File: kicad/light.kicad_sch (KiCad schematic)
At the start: 152 parts, among them J2 USB_C_Receptacle_USB2.0_16P, J3 Barrell Jack, J4 02x04, J5 SM03B-SRSS-TB, J6 SM03B-SRSS-TB, J9 Conn_01x09_MountingPin, Q1 IRLML6344, Q2 IRLML6344, Q3 IRLML6344, SW1 Boot, SW3 On/Off, SW4 Mode, U1 RP2350A-QFN60, U10 MAX6816, U2 TPS5405DR, U3 W25Q128JVS, U4 LBEE5KL1YN-814, U5 TPS2115ADRBR, U6 TPS2121RUXR, U7 HDC1080, U8 MAX6816, U9 MAX6816, Y1 ABM8-272-T3

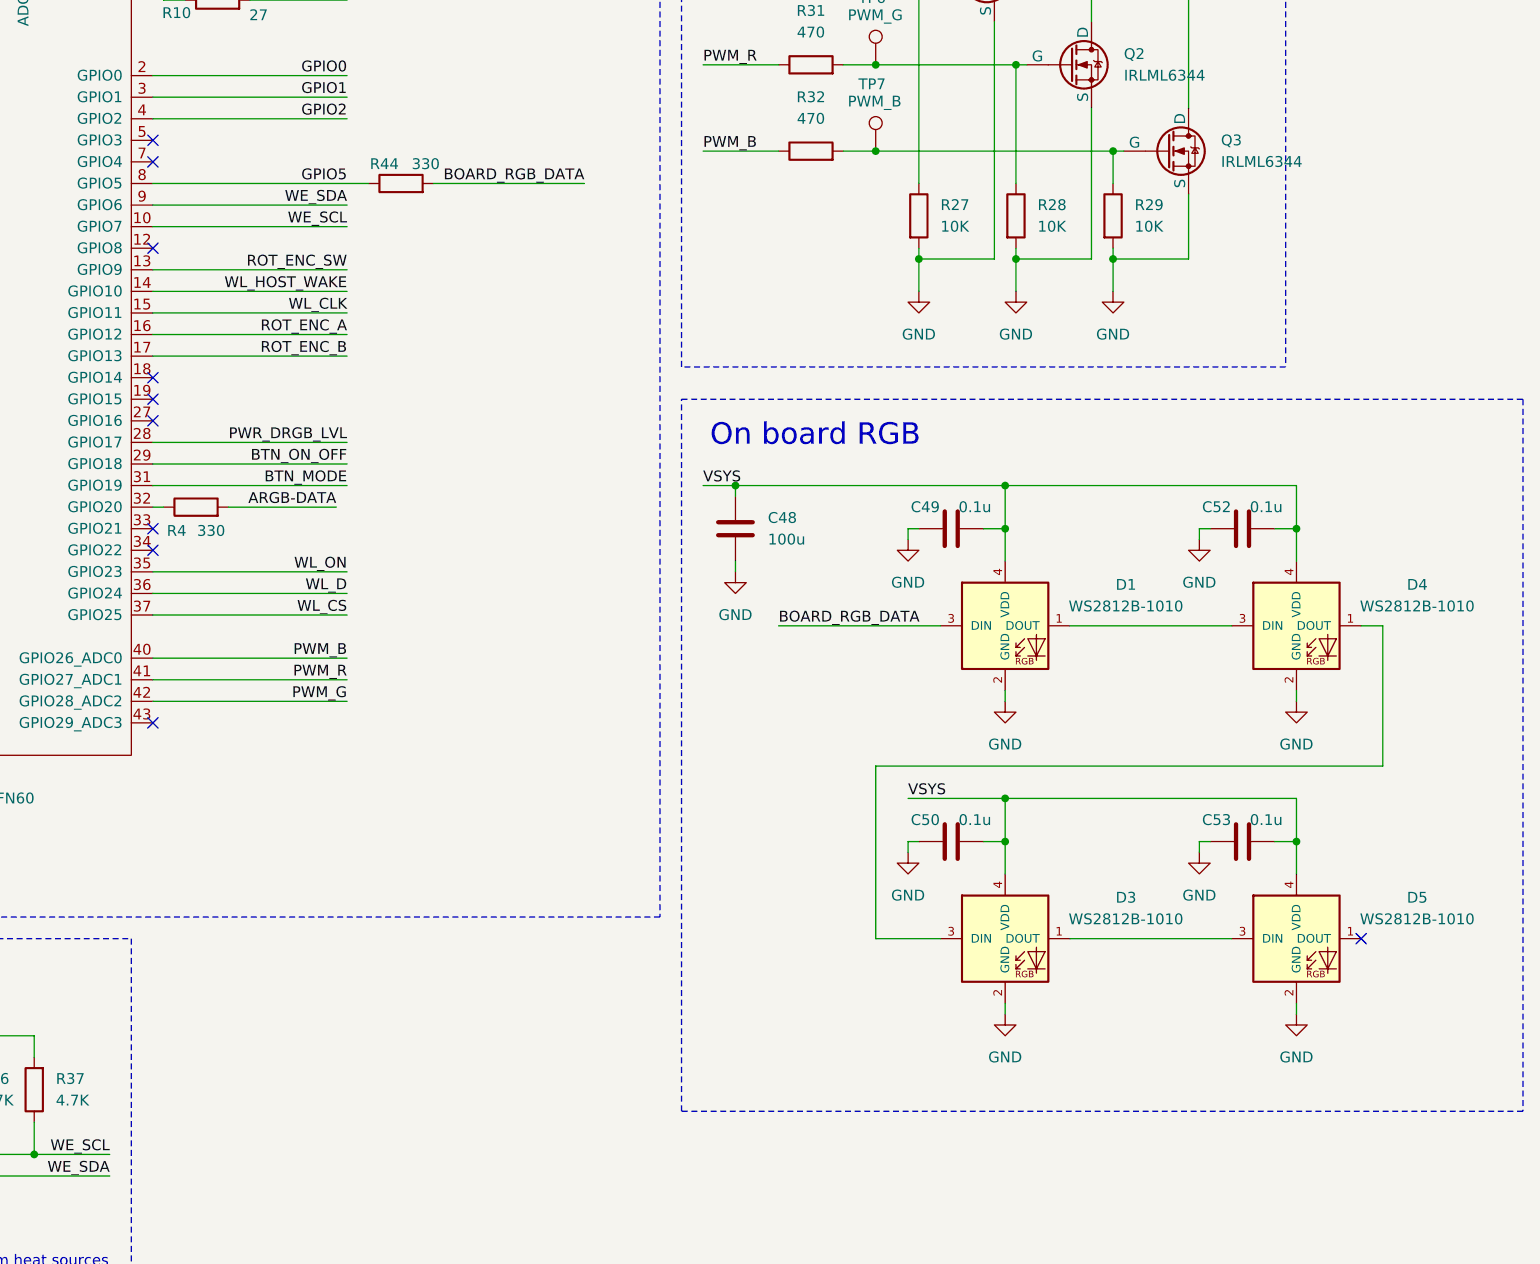
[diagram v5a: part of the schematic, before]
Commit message: change LEDs 1010 → 2020; general improvements
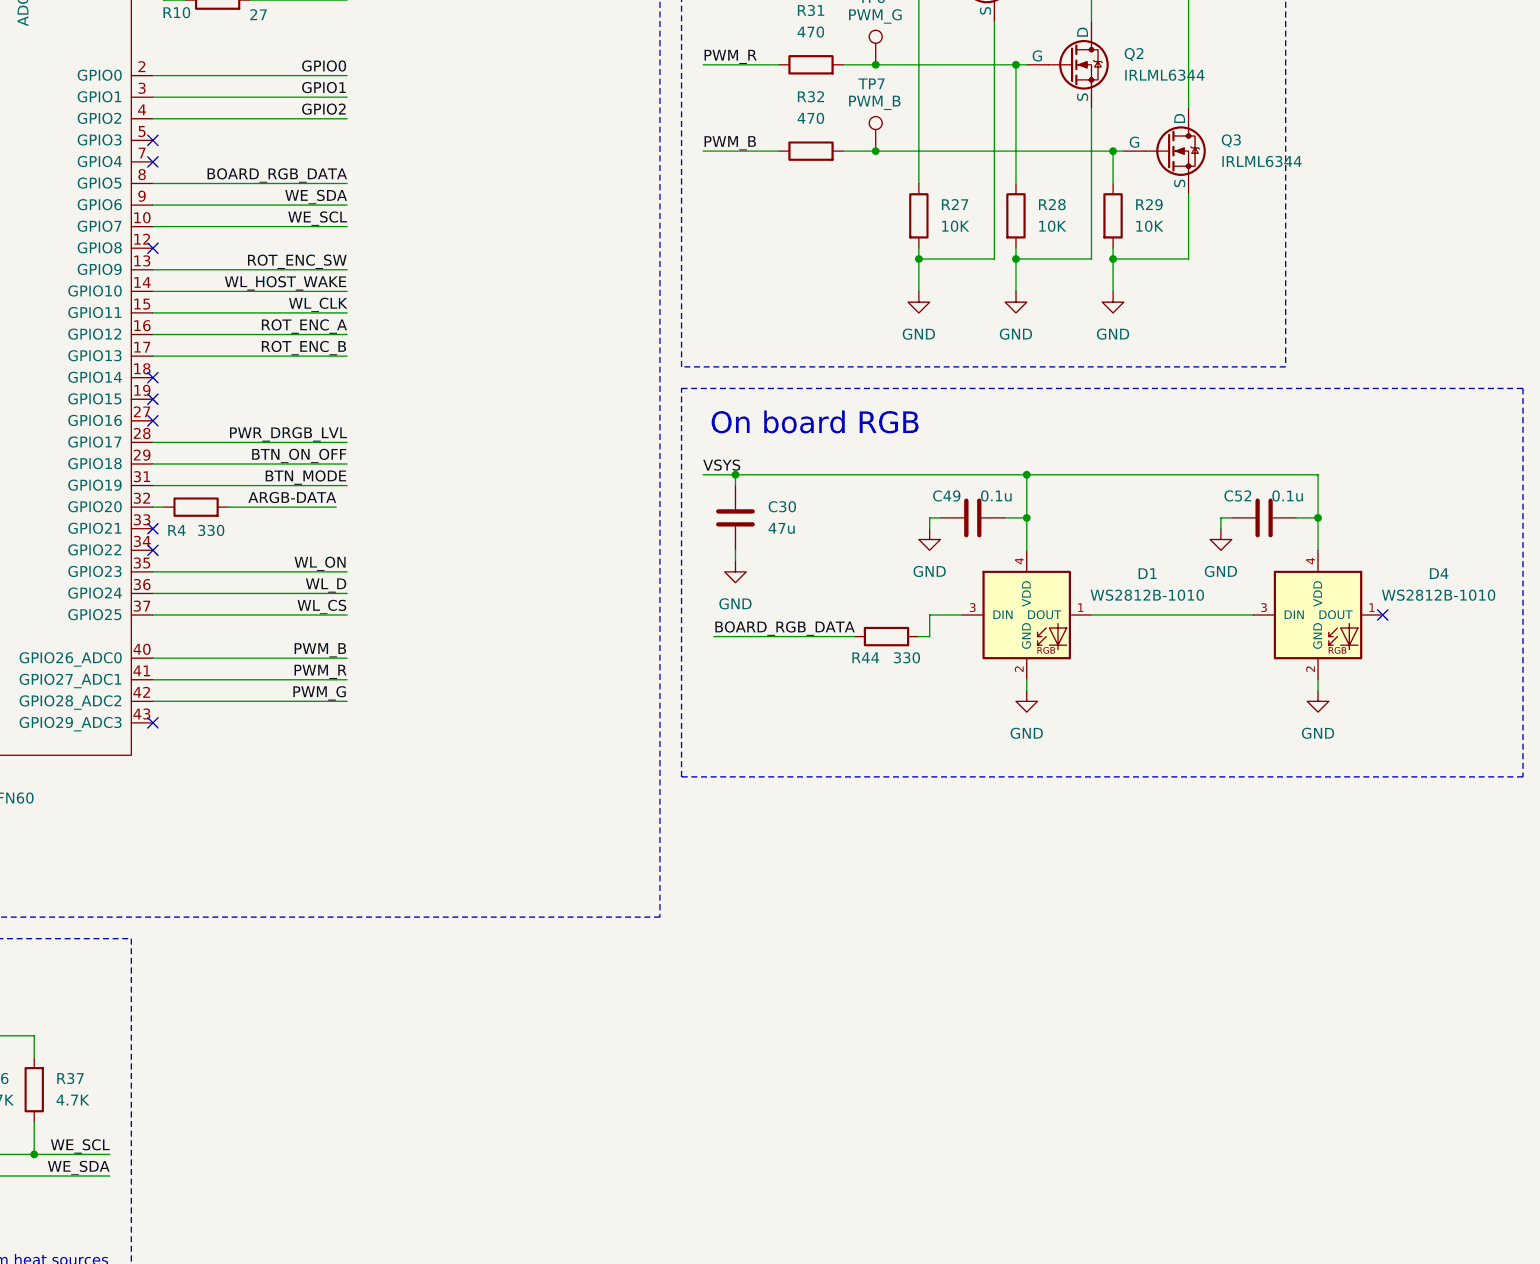
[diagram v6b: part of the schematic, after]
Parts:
- removed C48: 100u, Capacitor_SMD:C_0805_2012Metric, symbol Device:C
- removed C50, C53: 0.1u, Capacitor_SMD:C_0201_0603Metric, symbol Device:C
- removed D3, D5: WS2812B-1010, WS2812B_1010:WS2812B_1010, symbol WS2812C-2020:WS2812C-2020
- added C30: 47u, Capacitor_SMD:C_0402_1005Metric, symbol Device:C
- C16, C28: JLC C23733 -> C335103
- C22, C42, C46: footprint Capacitor_SMD:C_0201_0603Metric -> Capacitor_SMD:C_0402_1005Metric; JLC C92487 -> C15525
- C29: JLC C12530 -> C76933
- D1, D4: footprint WS2812B_1010:WS2812B_1010 -> WS2812B_1010:WS2812C-2020; JLC C15008 -> (none)
- R5: JLC C1002 -> C25871
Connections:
- net GPIO5 is gone; now on net BOARD_RGB_DATA: R44.1, U1.8 (GPIO5)
- net BOARD_RGB_DATA: no longer D1.3 (DIN), R44.2
- net GND: now also C30.2
- net VSYS: now also C30.1
- new net: D1.3 (DIN), R44.2
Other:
- moved on the sheet: C49, C52, D1, D4, R44

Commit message: general improvements
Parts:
- removed TP5: PWM_R, TestPoint:TestPoint_Pad_D1.0mm, symbol Connector:TestPoint
- removed TP6: PWM_G, TestPoint:TestPoint_Pad_D1.0mm, symbol Connector:TestPoint
- removed TP7: PWM_B, TestPoint:TestPoint_Pad_D1.0mm, symbol Connector:TestPoint
- removed TP9: V_RGB, TestPoint:TestPoint_Pad_D1.0mm, symbol Connector:TestPoint
- C30: footprint Capacitor_SMD:C_0402_1005Metric -> Capacitor_SMD:C_0603_1608Metric; JLC (none) -> C140782
- D1, D4: value WS2812B-1010 -> WS2812B-2020; JLC (none) -> C965555
- R26: JLC C473604 -> C25109

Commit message: detailing
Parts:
- added TP1: VBUS, TestPoint:TestPoint_Pad_D1.0mm, symbol Connector:TestPoint
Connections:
- net at D70.2 (A), D75.4 (VCC), J2.A4 (VBUS)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: now also TP1.1
- net LX2: now reaches L2.2, VR1.6 (LX2a), VR1.7 (LX2b)
- net LX1: now reaches L2.1, VR1.8 (LX1b), VR1.9 (LX1a)
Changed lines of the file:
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@@
 	)
 	(junction
+		(at 86.36 53.34)
+		(diameter 0)
+		(color 0 0 0 0)
+	)
+	(junction
 		(at 247.65 43.18)
 		(diameter 0)
@@
 	(wire
 		(pts
-			(xy 81.28 53.34) (xy 105.41 53.34)
+			(xy 81.28 53.34) (xy 86.36 53.34)
 		)
 		(stroke
@@
 	(wire
 		(pts
+			(xy 86.36 53.34) (xy 105.41 53.34)
+		)
+		(stroke
+			(width 0)
+			(type default)
+		)
+	)
+	(wire
+		(pts
 			(xy 260.35 224.79) (xy 260.35 227.33)
 		)
@@
 		)
 	)
+	(label "LX1"
+		(at 218.44 116.84 0)
+		(effects
+			(font
+				(size 1.27 1.27)
+			)
+			(justify left bottom)
+		)
+	)
 	(label "QSPI_SD0"
 		(at 255.27 361.95 0)
@@
 		)
 	)
+	(label "LX2"
+		(at 219.71 127 0)
+		(effects
+			(font
+				(size 1.27 1.27)
+			)
+			(justify left bottom)
+		)
+	)
 	(label "GPIO2"
 		(at 384.81 229.87 180)
@@
 					(unit 1)
 				)
+			)
+		)
+	)
+	(symbol
+		(lib_id "Connector:TestPoint")
+		(at 86.36 53.34 0)
+		(unit 1)
+		(exclude_from_sim no)
+		(in_bom yes)
+		(on_board yes)
+		(dnp no)
+		(fields_autoplaced yes)
+		(property "Reference" "TP1"
+			(at 88.9 48.7679 0)
+			(effects
+				(font
+					(size 1.27 1.27)
+				)
+				(justify left)
+			)
+		)
+		(property "Value" "VBUS"
+			(at 88.9 51.3079 0)
+			(effects
+				(font
+					(size 1.27 1.27)
+				)
+				(justify left)
+			)
+		)
+		(property "Footprint" "TestPoint:TestPoint_Pad_D1.0mm"
+			(at 91.44 53.34 0)
+			(effects
+				(font
+					(size 1.27 1.27)
+				)
+				(hide yes)
+			)
+		)
+		(property "Datasheet" "~"
+			(at 91.44 53.34 0)
+			(effects
+				(font
+					(size 1.27 1.27)
+				)
+				(hide yes)
+			)
+		)
+		(property "Description" "test point"
+			(at 86.36 53.34 0)
+			(effects
+				(font
+					(size 1.27 1.27)
+				)
+				(hide yes)
+			)
+		)
+		(pin "1"
+		)
+		(instances
+			(project ""
+				(path "/fbb17af3-099c-429d-b186-ab4e8e0fdddf"
+					(reference "TP1")
+					(unit 1)
+				)
